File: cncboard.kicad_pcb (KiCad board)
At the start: 2 copper layers, 125.1 x 99.9 mm, 263 parts, among them J1 Spindle, J10 12-45V, J11 Laser on/off/auto, J12 LASER_3PIN, J13 Laser_Out, J14 Laser_Vcc, J15 MOT, J16 MOT, J17 MOT, J18 Y_MIN, J19 Y_MAX, J2 SPINDLE_DIRECTION, J20 Z_MIN, J21 Z_MAX, J22 X_MIN, J23 X_MAX, J24 Controls, J3 Coolant_flood, J4 COOLANT_MIST, J5 EXP1, J6 EXP2, J7 ISP, J8 USB_B, J9 MOT, K1 G5Q1AEU5DC, K2 G5Q1AEU5DC, Q1 AO3400, Q2 AO3400, Q3 AO3400, Q4 AO3400, Q5 BSS138, Q6 AOD409, U1 74LS157, U10 LTV-827S, U2 ATmega2560-16AU, U3 FT232RL, U4 ADuM1201AR, U5 MAX5035BUSA, U6 74AUC1G17, U7 74AUC1G17, U8 LTV-827S, U9 LTV-827S, Y1 LFXTAL003240l

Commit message: Placement update
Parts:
- moved D20 56.9 mm to (143.7, 63.6), turned to 270 degrees
- moved D22 56.3 mm to (145.5, 60.0)
- moved C28 55.2 mm to (145.5, 63.6), turned to 270 degrees
- moved R10 54.8 mm to (147.2, 63.8), turned to 270 degrees
- moved C4 51.7 mm to (88.1, 74.0)
- moved R38 45.9 mm to (91.6, 84.3), turned to 180 degrees
- moved R39 45.0 mm to (91.6, 82.8), turned to 180 degrees
- moved R37 44.9 mm to (91.6, 85.8), turned to 180 degrees
- moved R36 44.6 mm to (91.6, 87.3), turned to 180 degrees
- moved J7 40.3 mm to (137.4, 106.8), turned to 270 degrees
- moved D21 38.8 mm to (123.6, 60.0)
- moved D19 38.5 mm to (121.7, 63.7), turned to 270 degrees
- moved C27 37.2 mm to (123.6, 63.5), turned to 270 degrees
- moved R9 33.7 mm to (125.3, 63.6), turned to 270 degrees
- moved C67 32.3 mm to (136.1, 97.8), turned to 270 degrees
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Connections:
- A1 pad 14: /Stepper X/DCO -> /Stepper Z/DCO
- A1 pad 15: /Stepper X/STEP -> /Stepper Z/STEP
- A1 pad 16: /Stepper X/DIR -> /Stepper Z/DIR
- A1 pad 9: /Stepper X/EN -> /Stepper Z/EN
- A3 pad 14: /Stepper Z/DCO -> /Stepper X/DCO
- A3 pad 15: /Stepper Z/STEP -> /Stepper X/STEP
- A3 pad 16: /Stepper Z/DIR -> /Stepper X/DIR
- A3 pad 9: /Stepper Z/EN -> /Stepper X/EN
- C52 pad 1: /inputs/CYCLE_START -> /inputs/SAFETY_DOOR
- C53 pad 1: /inputs/SAFETY_DOOR -> /inputs/CYCLE_START
- C54 pad 1: /inputs/SOFT_RESET -> /inputs/FEED_HOLD
- C55 pad 2: /inputs/FEED_HOLD -> /inputs/SOFT_RESET
- D36 pad 1: /Stepper Z/DCO -> /Stepper X/DCO
- D5 pad 1: /Stepper X/DCO -> /Stepper Z/DCO
- J7 pad 2: +5VD -> +5V
- JP10 pad 1: /Stepper Z/CS -> /Stepper X/CS
- JP2 pad 1: /Stepper X/CS -> /Stepper Z/CS
- R16 pad 2: /Stepper Z/EN -> /Stepper X/EN
- R26 pad 2: +5VD -> +5V
- R27 pad 2: +5VD -> +5V
- R28 pad 2: +5VD -> +5V
- R29 pad 2: +5VD -> +5V
- R30 pad 2: +5VD -> +5V
- R31 pad 2: +5VD -> +5V
- R32 pad 1: /inputs/CYCLE_START -> /inputs/SAFETY_DOOR
- R33 pad 1: /inputs/SAFETY_DOOR -> /inputs/CYCLE_START
- R34 pad 1: /inputs/SOFT_RESET -> /inputs/FEED_HOLD
- R35 pad 1: /inputs/FEED_HOLD -> /inputs/SOFT_RESET
- R36 pad 1: /inputs/CYCLE_START -> /inputs/SAFETY_DOOR
- R37 pad 1: /inputs/SAFETY_DOOR -> /inputs/CYCLE_START
- R38 pad 1: /inputs/SOFT_RESET -> /inputs/FEED_HOLD
- R39 pad 1: /inputs/FEED_HOLD -> /inputs/SOFT_RESET
- R6 pad 2: /Stepper X/EN -> /Stepper Z/EN
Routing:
- net +5VD: track 319.6 -> 134.2 mm, vias 12 -> 0
- net GND: track 547.3 -> 386.7 mm, vias 216 -> 143
- net /Stepper X/STEP: track 95.4 -> 0.20 mm, vias 5 -> 0
- net /Stepper Y/STEP: track 75.6 -> 0.00 mm, vias 6 -> 0
- net /Stepper X/DIR: track 72.8 -> 0.29 mm, vias 3 -> 0
- net /Stepper E0/CS: track 66.0 -> 0.00 mm, vias 4 -> 0
- net /mcu/MOSI: track 131.1 -> 68.8 mm, vias 2 -> 0
- net /Stepper X/EN: track 63.9 -> 2.17 mm, vias 8 -> 0
- net /Stepper E0/SCK: track 125.9 -> 68.2 mm, vias 10 -> 0
- net /mcu/MISO: track 127.0 -> 71.1 mm, vias 8 -> 0
- net /Stepper Z/DIR: track 54.2 -> 0.00 mm, vias 3 -> 0
- net /Stepper Z/STEP: track 53.1 -> 0.00 mm, vias 3 -> 0
- net /Stepper X/CS: track 52.5 -> 0.00 mm, vias 4 -> 0
- net /Stepper Z/CS: track 46.2 -> 0.00 mm, vias 4 -> 0
- net /mcu/LASER_PWM: track 45.7 -> 0.00 mm, vias 2 -> 0
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
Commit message: routing in progress
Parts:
- moved C64 69.1 mm to (68.2, 91.2), turned to 90 degrees
- moved C66 1.11 mm to (134.0, 96.7)
- moved C67 1.11 mm to (135.9, 96.7)
- moved C60 0.85 mm to (109.2, 97.3)
- moved R6 0.47 mm to (87.5, 63.5)
- moved JP5 0.20 mm to (97.2, 63.5)
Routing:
- net /mcu/MISO: track 71.1 -> 171.0 mm, vias 0 -> 9
- net /mcu/MOSI: track 68.8 -> 161.2 mm, vias 0 -> 3
- net /Stepper E0/SCK: track 68.2 -> 159.4 mm, vias 0 -> 9
- net Net-(C30-Pad2): track 0.00 -> 79.4 mm
- net /inputs/Y_MIN: track 2.32 -> 66.2 mm, vias 0 -> 4
- net /inputs/Y_MAX: track 4.97 -> 65.5 mm, vias 0 -> 4
- net /inputs/SOFT_RESET: track 12.5 -> 71.7 mm, vias 0 -> 3
- net /Stepper Z/DIR: track 0.00 -> 56.5 mm, vias 0 -> 2
- net /Stepper Z/STEP: track 0.00 -> 54.6 mm
- net /Stepper X/CS: track 0.00 -> 54.1 mm, vias 0 -> 2
- net /Stepper E0/CS: track 0.00 -> 50.2 mm, vias 0 -> 2
- net /mcu/COOLANT_FLOOD: track 0.00 -> 49.6 mm, vias 0 -> 4
- net /Stepper Y/STEP: track 0.00 -> 47.4 mm, vias 0 -> 2
- net /mcu/PC4: track 0.00 -> 46.7 mm, vias 0 -> 1
- net /mcu/STEP_E0: track 0.00 -> 46.6 mm, vias 0 -> 2
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
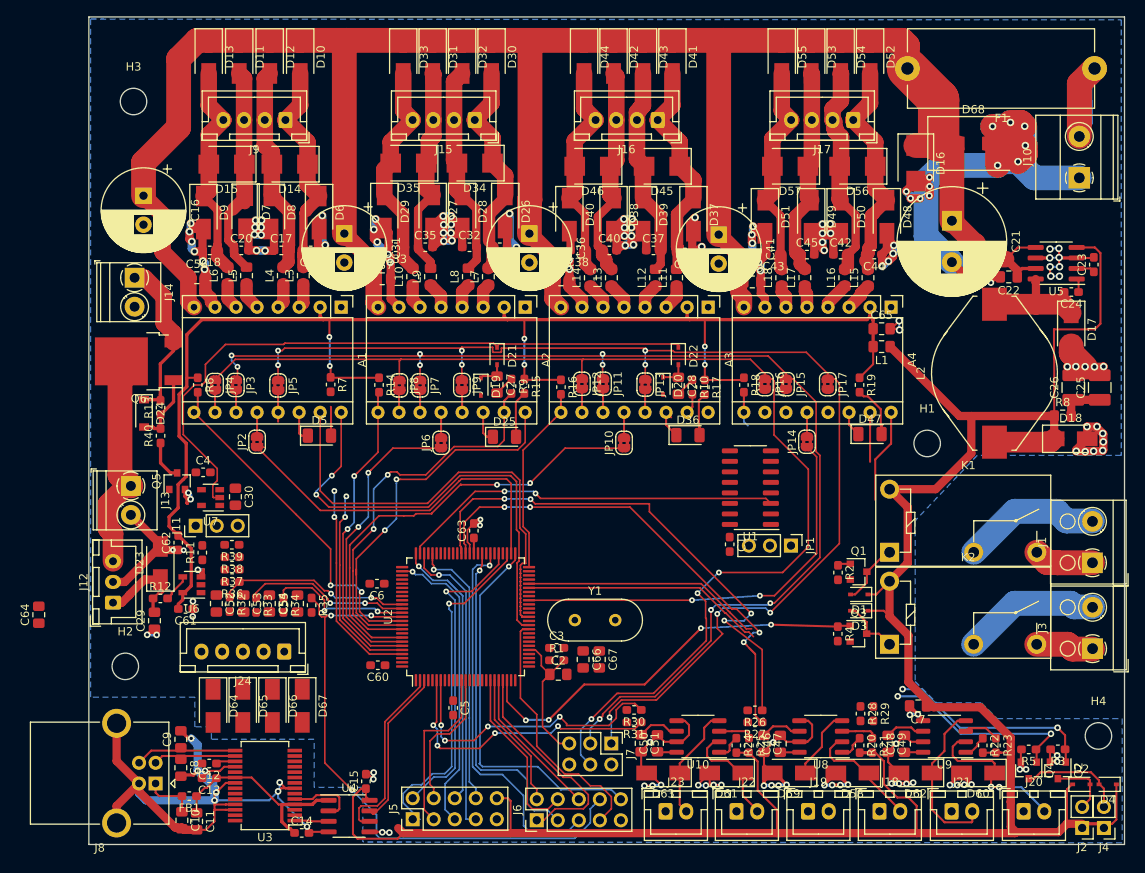
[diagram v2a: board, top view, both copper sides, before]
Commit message: Finish routing/nicifying V1
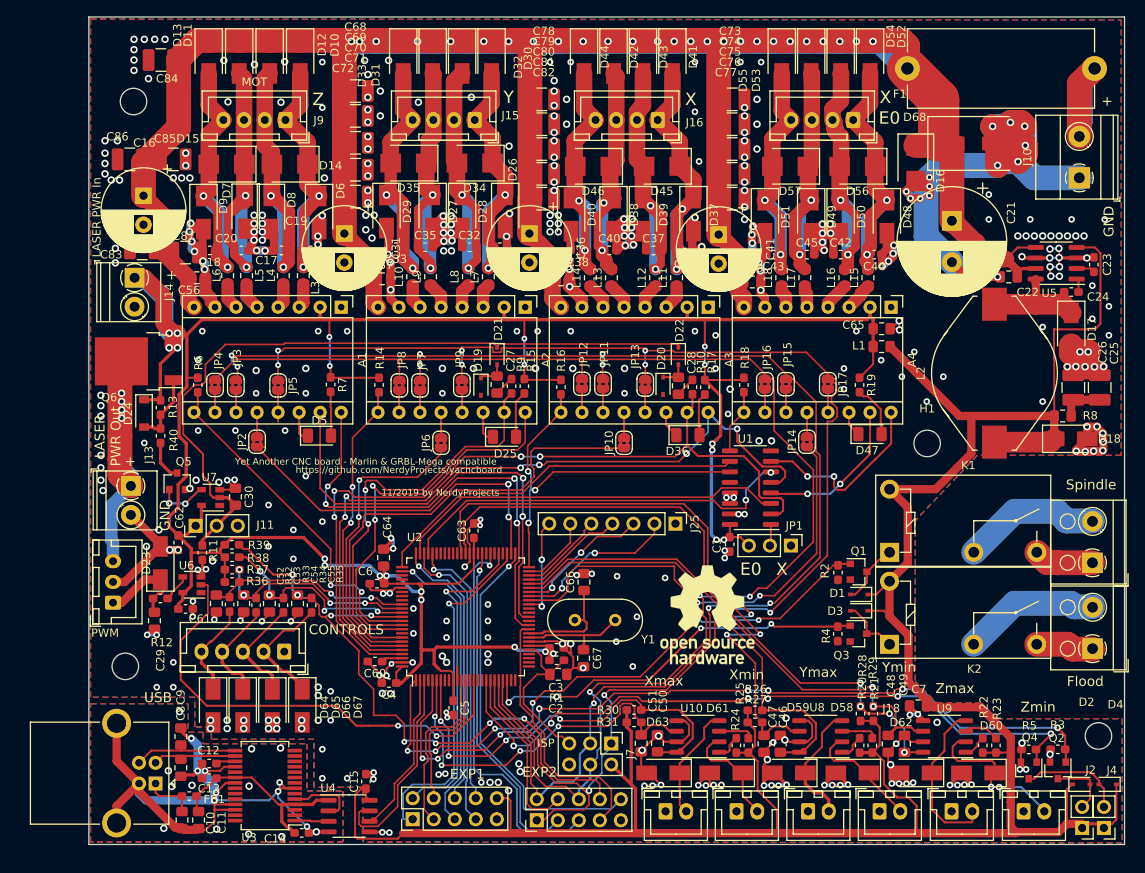
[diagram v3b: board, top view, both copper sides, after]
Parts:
- added C68: 10u/50V, Capacitor_SMD:C_1210_3225Metric_Pad1.42x2.65mm_HandSolder, F.Cu at (106.5, 28.0)
- added C69: 10u/50V, Capacitor_SMD:C_1210_3225Metric_Pad1.42x2.65mm_HandSolder, F.Cu at (106.5, 31.0)
- added C70: 10u/50V, Capacitor_SMD:C_1210_3225Metric_Pad1.42x2.65mm_HandSolder, F.Cu at (106.5, 34.2)
- added C71: 10u/50V, Capacitor_SMD:C_1210_3225Metric_Pad1.42x2.65mm_HandSolder, F.Cu at (106.5, 37.5)
- added C72: 10u/50V, Capacitor_SMD:C_1210_3225Metric_Pad1.42x2.65mm_HandSolder, F.Cu at (106.5, 40.8)
- added C73: 10u/50V, Capacitor_SMD:C_1210_3225Metric_Pad1.42x2.65mm_HandSolder, F.Cu at (152.0, 29.0)
- added C74: 10u/50V, Capacitor_SMD:C_1210_3225Metric_Pad1.42x2.65mm_HandSolder, F.Cu at (152.0, 32.0)
- added C75: 10u/50V, Capacitor_SMD:C_1210_3225Metric_Pad1.42x2.65mm_HandSolder, F.Cu at (152.0, 35.0)
- added C76: 10u/50V, Capacitor_SMD:C_1210_3225Metric_Pad1.42x2.65mm_HandSolder, F.Cu at (152.0, 38.0)
- added C77: 10u/50V, Capacitor_SMD:C_1210_3225Metric_Pad1.42x2.65mm_HandSolder, F.Cu at (152.0, 41.0)
- added C78: 10u/50V, Capacitor_SMD:C_1210_3225Metric_Pad1.42x2.65mm_HandSolder, F.Cu at (129.0, 29.0)
- added C79: 10u/50V, Capacitor_SMD:C_1210_3225Metric_Pad1.42x2.65mm_HandSolder, F.Cu at (129.0, 32.0)
- added C80: 10u/50V, Capacitor_SMD:C_1210_3225Metric_Pad1.42x2.65mm_HandSolder, F.Cu at (129.0, 35.0)
- added C81: 10u/50V, Capacitor_SMD:C_1210_3225Metric_Pad1.42x2.65mm_HandSolder, F.Cu at (129.0, 38.0)
- added C82: 10u/50V, Capacitor_SMD:C_1210_3225Metric_Pad1.42x2.65mm_HandSolder, F.Cu at (129.0, 41.0)
- added C83: 10u/50V, Capacitor_SMD:C_1210_3225Metric_Pad1.42x2.65mm_HandSolder, F.Cu at (80.8, 47.0)
- added C84: 10u/50V, Capacitor_SMD:C_1210_3225Metric_Pad1.42x2.65mm_HandSolder, F.Cu at (83.0, 24.2)
- added C85: 10u/50V, Capacitor_SMD:C_1210_3225Metric_Pad1.42x2.65mm_HandSolder, F.Cu at (84.5, 36.2)
- added C86: 10u/50V, Capacitor_SMD:C_1210_3225Metric_Pad1.42x2.65mm_HandSolder, F.Cu at (79.2, 36.2)
- added C87: 10u/50V, Capacitor_SMD:C_1210_3225Metric_Pad1.42x2.65mm_HandSolder, F.Cu at (86.0, 47.5)
- added J25: Conn_01x07, Connector_PinHeader_2.54mm:PinHeader_1x07_P2.54mm_Vertical, F.Cu at (145.2, 80.2)
- added REF**: OSHW-Logo_11.4x12mm_SilkScreen, Symbol:OSHW-Logo_11.4x12mm_SilkScreen, F.Cu at (149.0, 91.2)
- moved C64 42.2 mm to (109.9, 84.3)
- moved C4 33.9 mm to (110.5, 99.5), turned to 180 degrees
- moved C66 9.35 mm to (134.1, 87.3), turned to 90 degrees
- moved C67 1.91 mm to (134.1, 96.5)
- moved C60 0.57 mm to (108.8, 96.9)
- moved C9 0.35 mm to (85.4, 106.0)
- moved C11 0.28 mm to (87.5, 116.0)
- moved D29 0.27 mm to (110.2, 42.5)
- moved D40 0.22 mm to (132.6, 42.9)
- moved R25 0.08 mm to (153.9, 107.0)
- moved D46 0.07 mm to (135.2, 37.1)
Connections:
- C12 pad 1: (no net) -> Net-(C12-Pad1)
- C12 pad 2: (no net) -> Net-(C10-Pad2)
- U2 pad 41: (no net) -> /mcu/PL6
- U2 pad 43: (no net) -> Net-(J25-Pad2)
- U2 pad 44: (no net) -> Net-(J25-Pad3)
- U2 pad 47: (no net) -> Net-(J25-Pad4)
- U2 pad 48: (no net) -> Net-(J25-Pad5)
- U2 pad 49: (no net) -> Net-(J25-Pad6)
- U3 pad 17: (no net) -> Net-(C12-Pad1)
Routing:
- net +5VD: track 174.3 -> 308.8 mm, vias 6 -> 19
- net /mcu/SPINDLE_DIRECTION: track 25.2 -> 98.1 mm, vias 2 -> 8
- net /mcu/SPINDLE_ENABLE: track 1.56 -> 73.2 mm, vias 0 -> 6
- net +VDC: track 269.2 -> 338.6 mm, vias 0 -> 26
- net /Stepper X/STEP: track 28.1 -> 96.8 mm, vias 2 -> 4
- net /Stepper X/DIR: track 24.6 -> 90.2 mm, vias 2 -> 6
- net /mcu/COOLANT_MIST: track 24.6 -> 83.8 mm, vias 2 -> 6
- net /mcu/LASER_PWM: track 0.00 -> 57.0 mm, vias 0 -> 2
- net /mcu/DIR_E0: track 0.00 -> 48.7 mm, vias 0 -> 2
- net /mcu/EN_E0: track 0.00 -> 45.9 mm
- net GND: track 393.3 -> 426.8 mm, vias 145 -> 403
- net /inputs/Z_MIN: track 31.5 -> 62.0 mm, vias 0 -> 4
- net +5V: track 285.5 -> 315.0 mm
- net /inputs/Z_MAX: track 34.4 -> 62.7 mm, vias 0 -> 2
- net /Stepper X/EN: track 23.1 -> 49.0 mm, vias 0 -> 3
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- added copper zone on F.Cu, net GND
- added copper zone on B.Cu, net Net-(C10-Pad2)
- added copper zone on F.Cu, net Net-(C10-Pad2)
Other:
- net class 230V: clearance 2.3 -> 2
- board text added: "+"
- board text added: "11/2019 by NerdyProjects"
- board text added: "CONTROLS"
- board text added: "E0"
- board text added: "EXP1"
- board text added: "EXP2"
- board text added: "Flood"
- board text added: "GND"
- board text added: "ISP"
- board text added: "LASER PWR In"
- board text added: "LASER PWR Out"
- board text added: "PWM"
- board text added: "Spindle"
- board text added: "USB"
- board text added: "X"
- board text added: "Xmax"
- board text added: "Xmin"
- board text added: "Y"
- board text added: "Yet Another CNC board - Marlin & GRBL-Mega compatible"
- board text added: "Ymax"
- board text added: "Ymin"
- board text added: "Z"
- board text added: "Zmax"
- board text added: "Zmin"
- board text added: "https://github.com/NerdyProjects/yacncboard"

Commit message: Silk screen adjustments
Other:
- board text added: "(depends on stepper driver!)"
- board text added: "12-50V"
- board text added: "TMC2130 or A4988 compatible drivers"
- board text added: "open all bridges if stepper driver has no SPI"
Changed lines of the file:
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@@
   (general
     (thickness 1.6)
-    (drawings 35)
+    (drawings 39)
     (tracks 3375)
     (zones 0)
@@
   (page A4)
   (layers
-    (0 F.Cu signal)
+    (0 F.Cu signal hide)
     (31 B.Cu signal)
     (32 B.Adhes user)
@@
     (tags "mounting hole 3.2mm no annular m3")
     (attr virtual)
-    (fp_text reference H1 (at 0 -4.2) (layer F.SilkS)
+    (fp_text reference H1 (at 0 -4.2) (layer F.SilkS) hide
       (effects (font (size 1 1) (thickness 0.15)))
     )
@@
     (descr "CP, Radial series, Radial, pin pitch=5.00mm, , diameter=13mm, Electrolytic Capacitor")
     (tags "CP Radial series Radial pin pitch 5.00mm  diameter 13mm Electrolytic Capacitor")
-    (fp_text reference C21 (at -0.9626 -7.1634 90) (layer F.SilkS)
+    (fp_text reference C21 (at -3.1626 -5.9634 90) (layer F.SilkS)
       (effects (font (size 1 1) (thickness 0.15)))
     )
@@
     )
   )
+  (gr_text "TMC2130 or A4988 compatible drivers" (at 102 57.75) (layer F.SilkS)
+    (effects (font (size 0.8 0.8) (thickness 0.1)))
+  )
+  (gr_text "open all bridges if stepper driver has no SPI" (at 103.25 58.75) (layer F.SilkS)
+    (effects (font (size 0.8 0.8) (thickness 0.1)))
+  )
+  (gr_text "(depends on\nstepper driver!)" (at 191.25 43.75) (layer F.SilkS)
+    (effects (font (size 0.8 0.8) (thickness 0.1)))
+  )
+  (gr_text 12-50V (at 191 42.25) (layer F.SilkS)
+    (effects (font (size 1 1) (thickness 0.15)))
+  )
   (gr_text https://github.com/NerdyProjects/yacncboard (at 111.75 73.75) (layer F.SilkS)

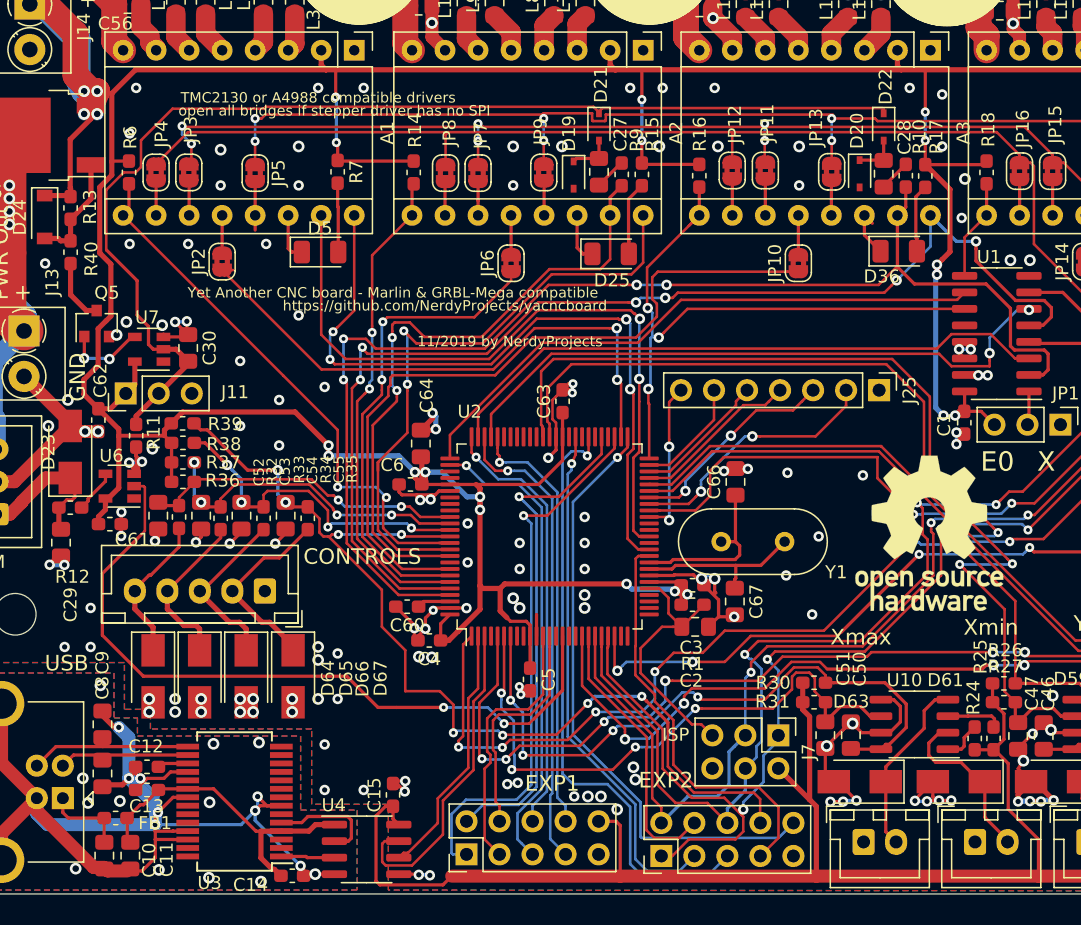
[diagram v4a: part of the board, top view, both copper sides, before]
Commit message: add autoreset and USB GND bridge
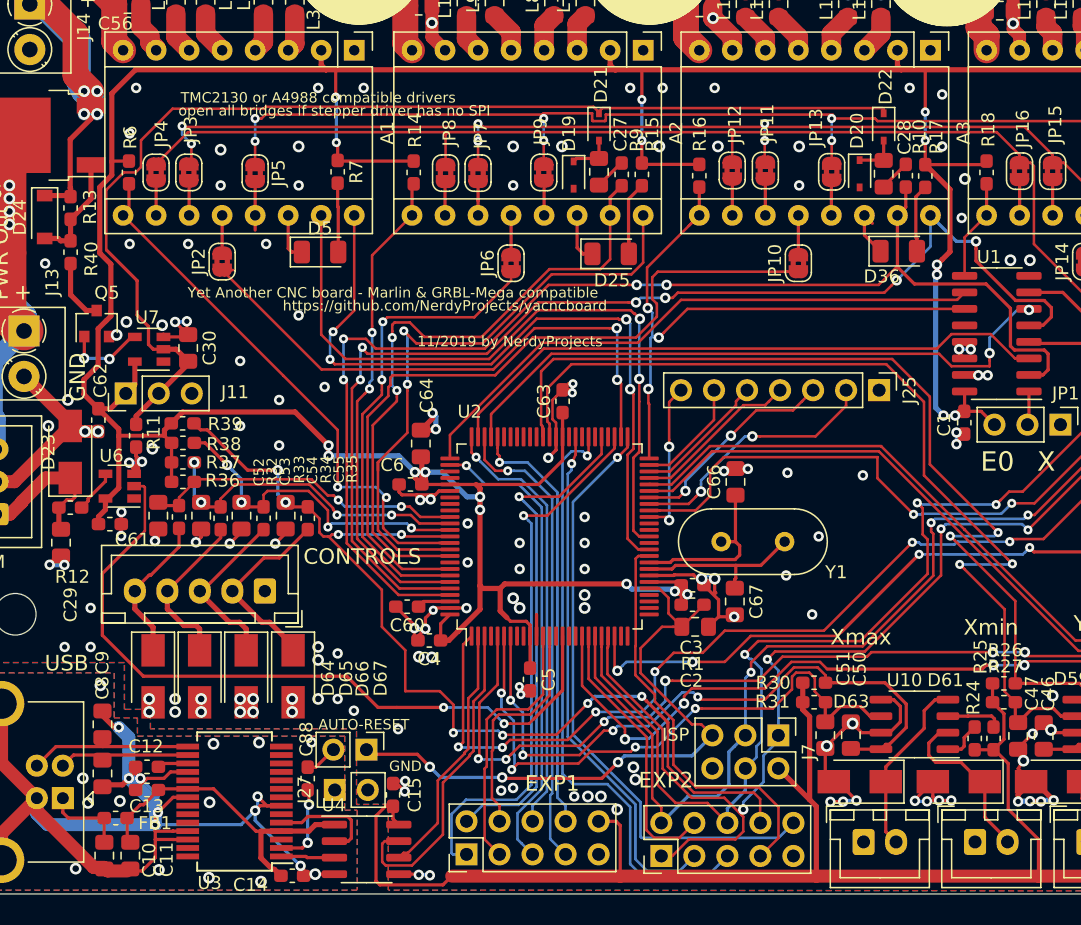
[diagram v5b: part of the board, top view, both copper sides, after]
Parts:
- removed REF**: OSHW-Logo_11.4x12mm_SilkScreen, Symbol:OSHW-Logo_11.4x12mm_SilkScreen
- added C88: 100n, Capacitor_SMD:C_0603_1608Metric_Pad1.05x0.95mm_HandSolder, F.Cu at (101.2, 110.1)
- added J26: AUTORESET, Connector_PinHeader_2.54mm:PinHeader_1x02_P2.54mm_Vertical, F.Cu at (105.7, 107.9)
- added J27: GND_BRIDGE, Connector_PinHeader_2.54mm:PinHeader_1x02_P2.54mm_Vertical, F.Cu at (103.3, 111.0)
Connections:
- U3 pad 2: (no net) -> /usb/DTR
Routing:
- net /mcu/RESET: track 20.1 -> 48.3 mm, vias 0 -> 3
- net /usb/DTR: track 0.00 -> 6.45 mm, vias 0 -> 2
- net Net-(C88-Pad1): track 0.00 -> 2.95 mm
- net Net-(D24-Pad1): track 34.1 -> 32.4 mm
- net Net-(C10-Pad2): vias 20 -> 21
- net GND: vias 403 -> 402
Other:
- board text added: "AUTO-RESET"
